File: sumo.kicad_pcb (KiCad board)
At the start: 2 copper layers, 76.2 x 94 mm, 55 parts, among them Q1 BPW40, Q2 BPW40, SW1 SW_Push, SW2 SW_DIP_x01, SW3 SW_DIP_x01, SW4 SW_DIP_x01, T1 Screw_Terminal_01x04, T2 Screw_Terminal_01x04, T3 Screw_Terminal_01x04, T4 Screw_Terminal_01x04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

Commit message: save changes
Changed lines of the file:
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@@
 			)
 		)
-		(pad "1" thru_hole rect
+		(pad "1" thru_hole circle
 			(at 0 0 270)
-			(size 1.4 1.4)
-			(drill 0.7)
+			(size 1.778 1.778)
+			(drill 0.8)
 			(layers "*.Cu" "*.Mask")
 			(remove_unused_layers no)
@@
 			)
 		)
-		(pad "1" thru_hole rect
+		(pad "1" thru_hole circle
 			(at 0 0 270)
-			(size 1.4 1.4)
-			(drill 0.7)
+			(size 1.778 1.778)
+			(drill 0.8)
 			(layers "*.Cu" "*.Mask")
 			(remove_unused_layers no)
@@
 			)
 		)
-		(pad "1" thru_hole rect
+		(pad "1" thru_hole circle
 			(at 0 0)
-			(size 1.4 1.4)
-			(drill 0.7)
+			(size 1.778 1.778)
+			(drill 0.8)
 			(layers "*.Cu" "*.Mask")
 			(remove_unused_layers no)

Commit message: finishing touches
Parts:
- moved T5 1.27 mm to (154.9, 83.8)
- moved T3 1.27 mm to (176.5, 114.3)
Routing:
- net Net-(T5-Pin_1): track 33.7 -> 32.4 mm
- net Net-(T5-Pin_4): track 21.2 -> 19.9 mm
- net Net-(T5-Pin_3): track 23.7 -> 22.4 mm
- net Net-(T5-Pin_2): track 31.9 -> 30.7 mm
- net Net-(C4-Pad1): track 48.8 -> 49.9 mm
- net Net-(U4-Pad2): track 35.7 -> 36.6 mm
- net Net-(T3-Pin_4): track 6.89 -> 6.36 mm
- net Net-(T3-Pin_3): track 7.41 -> 6.89 mm
- net Net-(T3-Pin_2): track 6.89 -> 7.41 mm
- net Net-(T3-Pin_1): track 6.36 -> 6.89 mm
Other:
- board text added: "Vacuum Cleaner Motherboard"
- board text added: "Vacuum Cleaner Sensor board"

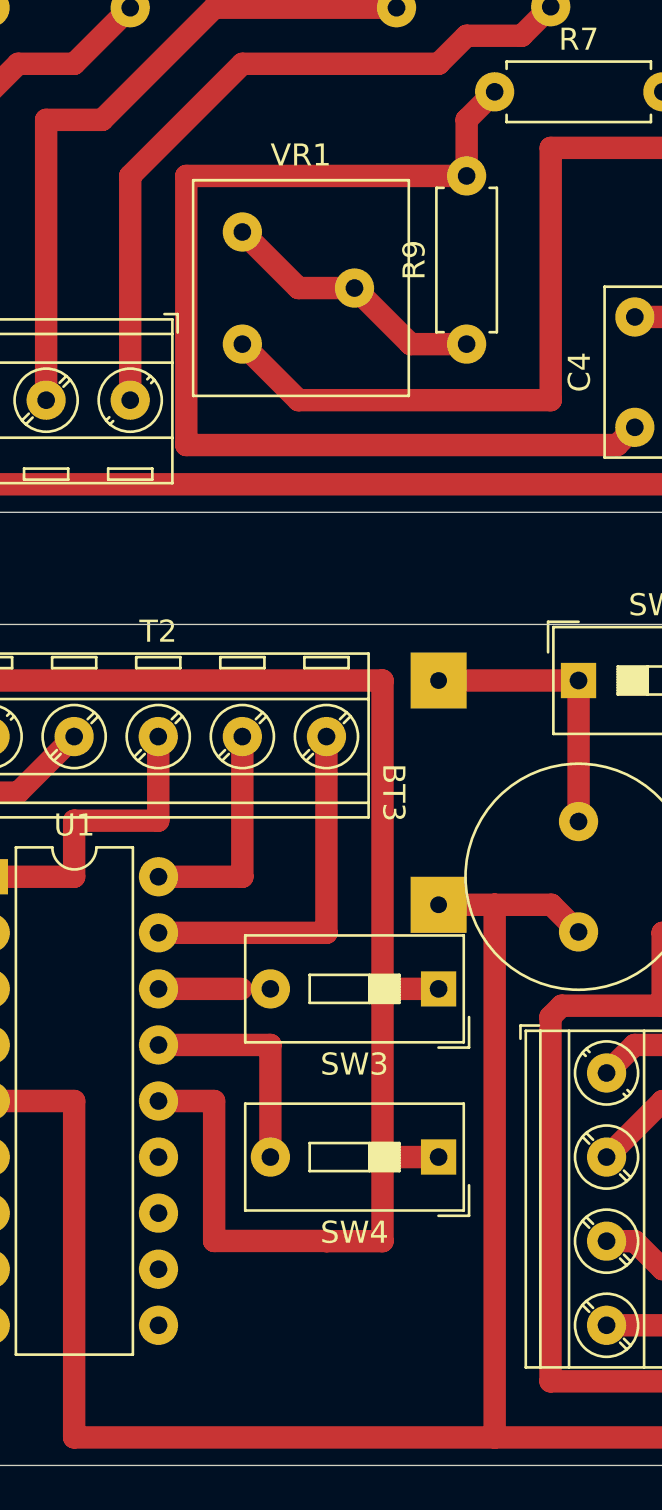
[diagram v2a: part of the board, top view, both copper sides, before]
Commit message: add pull up resistor to switch inputs
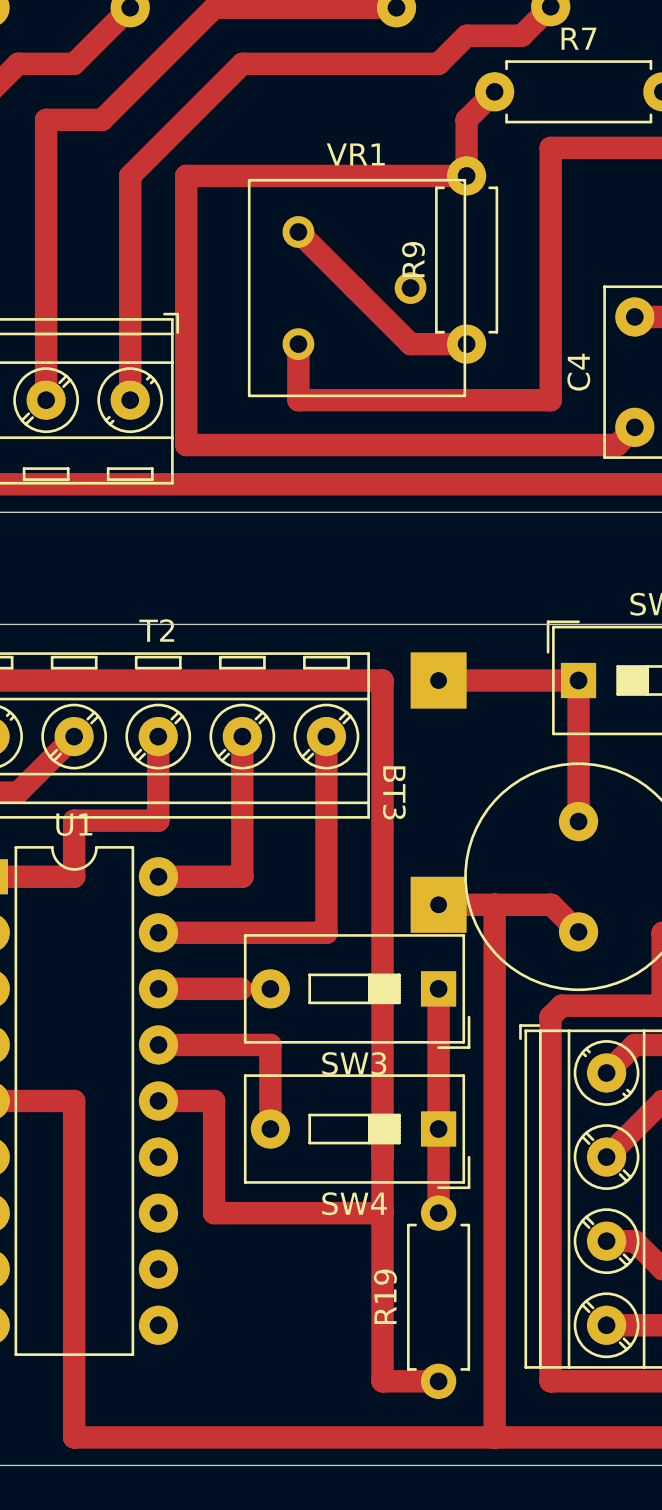
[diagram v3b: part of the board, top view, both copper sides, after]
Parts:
- added R19: 4.7k, Resistor_THT:R_Axial_DIN0207_L6.3mm_D2.5mm_P7.62mm_Horizontal, F.Cu at (168.9, 128.3)
- moved VR1 2.54 mm to (162.6, 81.3)
- moved SW4 1.27 mm to (168.9, 116.8)
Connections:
- SW3 pad 1: +5V -> Net-(R19-Pad2)
- SW4 pad 1: +5V -> Net-(R19-Pad2)
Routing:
- net Net-(R19-Pad2): track 0.00 -> 10.2 mm
- net +5V: track 91.2 -> 95.0 mm
- net Net-(R9-Pad1): track 12.3 -> 9.72 mm
- net Net-(U1-CLKOUT/OSC2/RA6): track 10.1 -> 8.88 mm
- net Net-(U4-Pad2): track 36.6 -> 35.6 mm

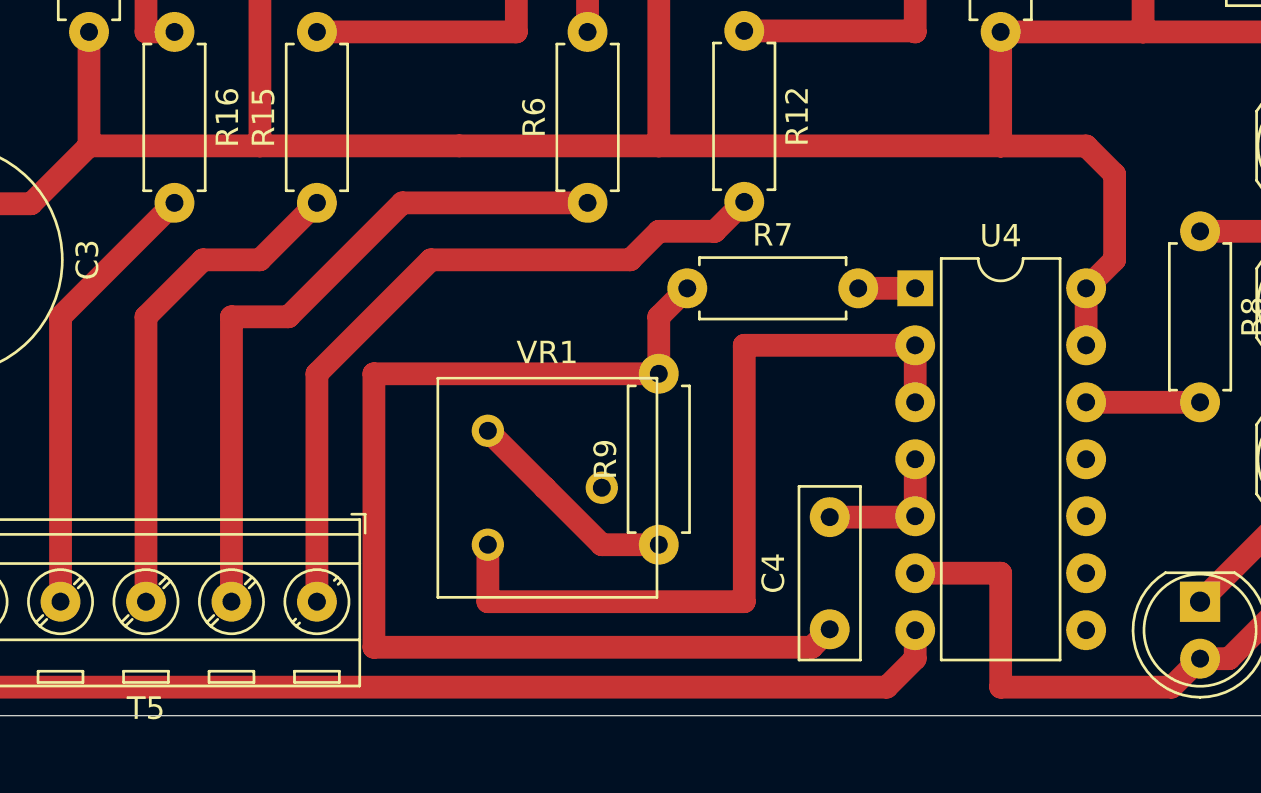
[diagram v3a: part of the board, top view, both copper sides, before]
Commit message: change potentiometer footprint
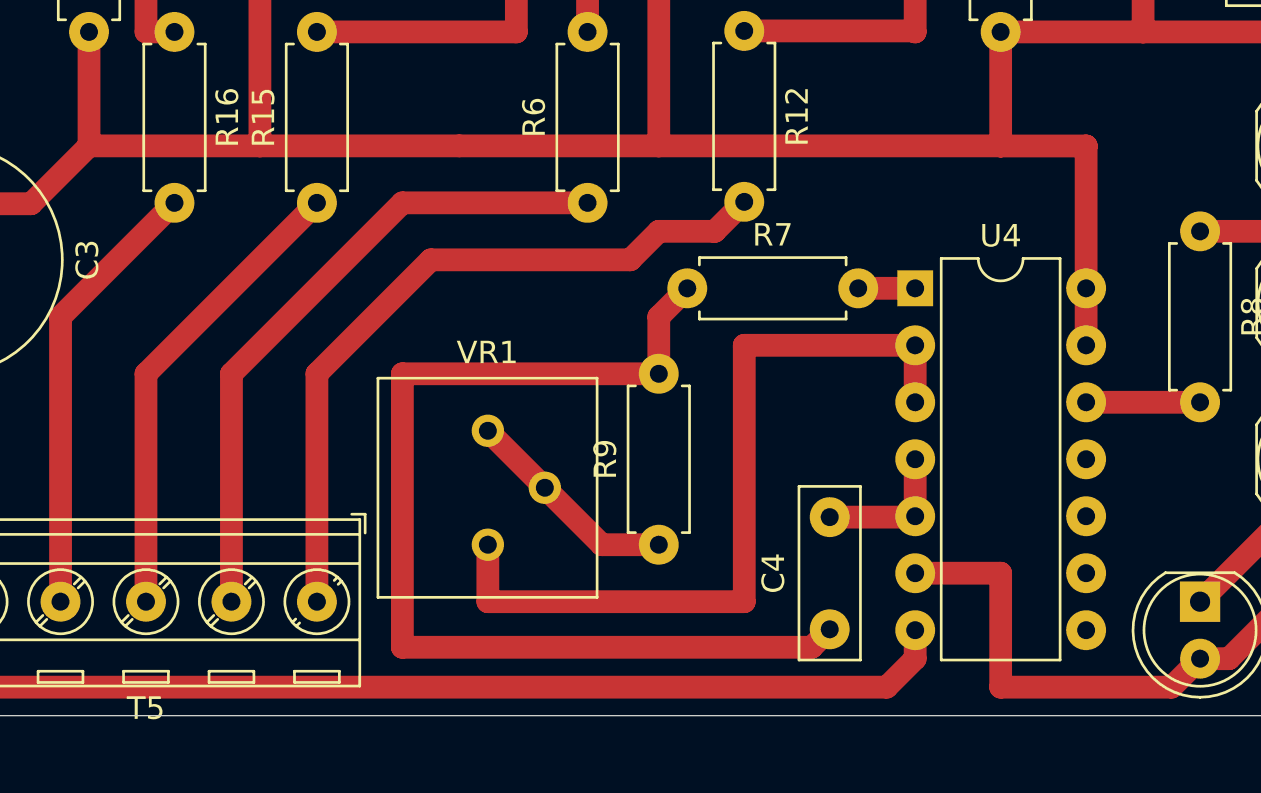
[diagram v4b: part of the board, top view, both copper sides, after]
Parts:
- R19: value 4.7k -> 1k
- VR1: footprint Potentiometer_THT:Potentiometer_Bourns_3386F_Vertical -> Potentiometer_THT:Potentiometer_Bourns_3386P_Vertical
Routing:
- net Net-(C4-Pad1): track 49.9 -> 47.3 mm
- net Net-(T5-Pin_3): track 22.4 -> 20.9 mm
- net Net-(T5-Pin_2): track 30.7 -> 29.2 mm
- net +6V: track 150.9 -> 149.9 mm

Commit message: ground plane
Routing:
- net GNDREF: track 358.0 -> 0.08 mm
- net Net-(D3-A): track 44.6 -> 47.5 mm
- net +6V: track 149.9 -> 147.2 mm
- net Net-(D3-K): track 25.7 -> 27.9 mm
- net Net-(Q2-C): track 24.4 -> 26.7 mm
- net Net-(Q1-C): track 15.3 -> 17.1 mm
- net Net-(T2-Pin_2): track 14.7 -> 16.3 mm
- net Net-(U1-CLKIN/OSC1/RA7): track 3.76 -> 5.07 mm
- net +5V: track 95.0 -> 93.8 mm
- net Net-(U3-VCC1): track 85.6 -> 86.6 mm
- net Net-(U1-~{MCLR}/Vpp/RA5): track 13.2 -> 14.0 mm
- net Net-(C4-Pad1): track 47.3 -> 48.1 mm
- added copper zone on F.Cu, net GNDREF

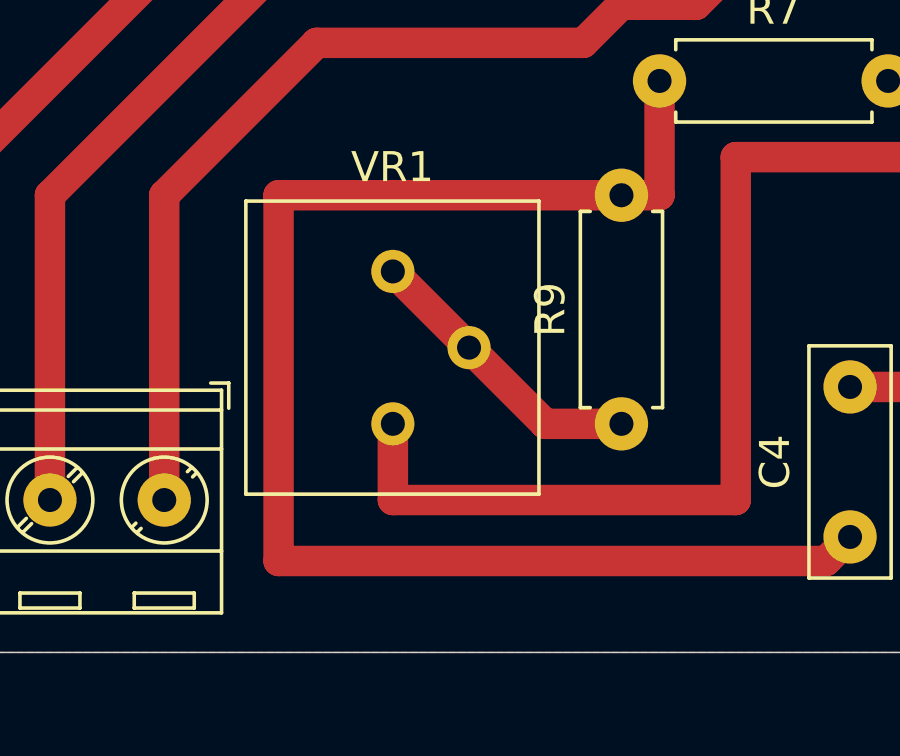
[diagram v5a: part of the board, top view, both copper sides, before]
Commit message: change potentiometer pads
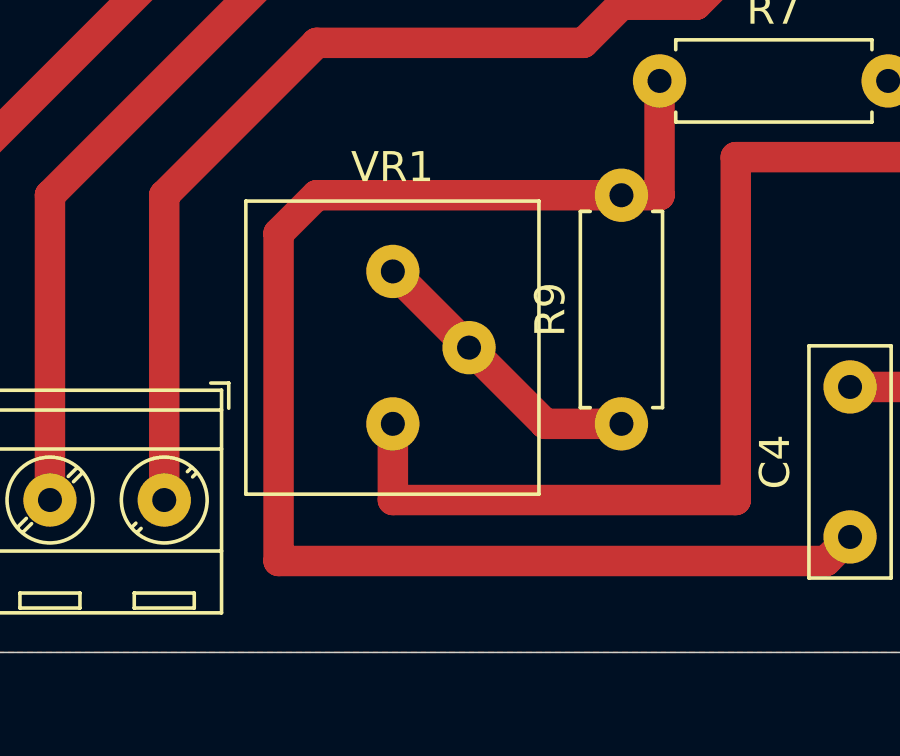
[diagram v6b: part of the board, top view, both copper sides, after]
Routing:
- net Net-(C4-Pad1): track 48.1 -> 47.3 mm
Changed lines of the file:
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@@
 		(pad "1" thru_hole circle
 			(at 0 0)
-			(size 1.44 1.44)
+			(size 1.778 1.778)
 			(drill 0.8)
 			(layers "*.Cu" "*.Mask")
@@
 		(pad "2" thru_hole circle
 			(at 2.54 -2.54)
-			(size 1.44 1.44)
+			(size 1.778 1.778)
 			(drill 0.8)
 			(layers "*.Cu" "*.Mask")
@@
 		(pad "3" thru_hole circle
 			(at 0 -5.08)
-			(size 1.44 1.44)
+			(size 1.778 1.778)
 			(drill 0.8)
 			(layers "*.Cu" "*.Mask")
@@
 	)
 	(segment
-		(start 176.998 85.852)
-		(end 177.8 85.05)
+		(start 158.75 85.852)
+		(end 176.998 85.852)
 		(width 1.016)
 		(layer "F.Cu")
@@
 	)
 	(segment
-		(start 158.75 85.852)
-		(end 176.998 85.852)
+		(start 160.02 73.66)
+		(end 158.75 74.93)
+		(width 1.016)
+		(layer "F.Cu")
+		(net 25)
+	)
+	(segment
+		(start 170.18 73.66)
+		(end 160.02 73.66)
 		(width 1.016)
 		(layer "F.Cu")
@@
 	)
 	(segment
-		(start 158.75 73.66)
-		(end 158.75 85.852)
+		(start 176.998 85.852)
+		(end 177.8 85.05)
 		(width 1.016)
 		(layer "F.Cu")
@@
 	)
 	(segment
-		(start 170.18 73.66)
-		(end 158.75 73.66)
+		(start 158.75 74.93)
+		(end 158.75 85.852)
 		(width 1.016)
 		(layer "F.Cu")

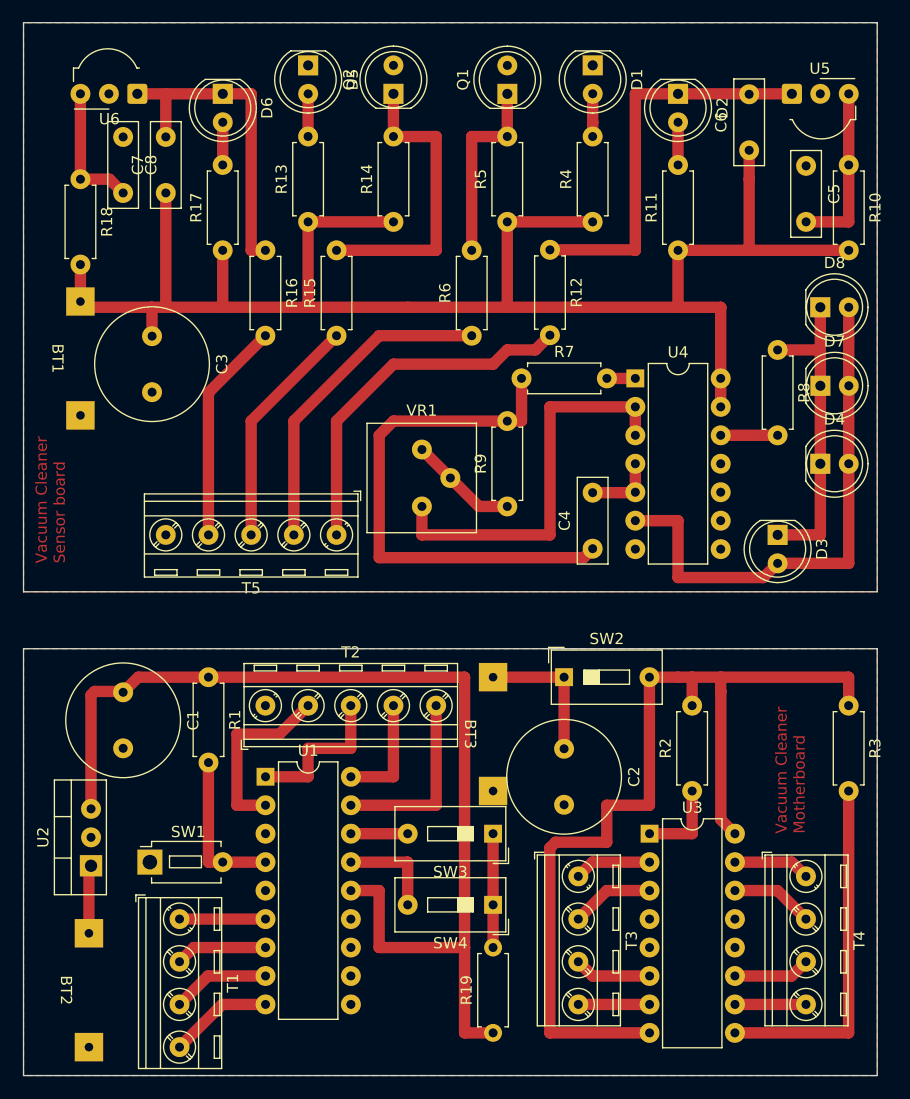
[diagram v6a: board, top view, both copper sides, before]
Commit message: remove ground plane
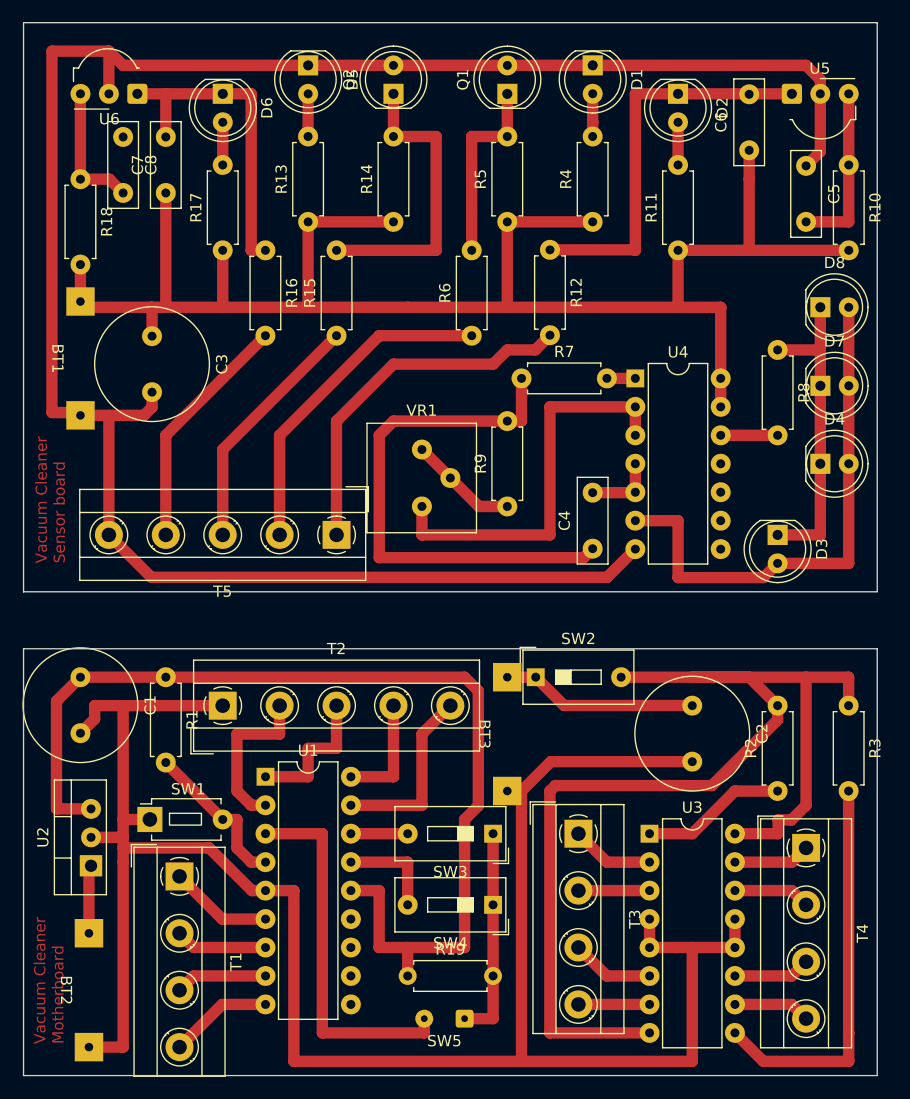
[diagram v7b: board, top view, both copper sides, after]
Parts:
- added SW5: SW_DIP_x01, Connector_Wire:SolderWire-0.1sqmm_1x02_P3.6mm_D0.4mm_OD1mm, F.Cu at (166.4, 127.0)
- T1, T3, T4: footprint TerminalBlock_MetzConnect:TerminalBlock_MetzConnect_Type086_RT03404HBLC_1x04_P3.81mm_Horizontal -> TerminalBlock_MetzConnect:TerminalBlock_MetzConnect_Type101_RT01604HBWC_1x04_P5.08mm_Horizontal
- T2, T5: value Screw_Terminal_01x04 -> Screw_Terminal_01x05; footprint TerminalBlock_MetzConnect:TerminalBlock_MetzConnect_Type086_RT03405HBLC_1x05_P3.81mm_Horizontal -> TerminalBlock_MetzConnect:TerminalBlock_MetzConnect_Type101_RT01605HBWC_1x05_P5.08mm_Horizontal
- moved C2 12.1 mm to (186.7, 99.1)
- moved R19 9.16 mm to (161.3, 123.2), turned to 0 degrees
- moved R2 7.63 mm to (194.3, 106.7)
- moved C1 4.04 mm to (132.1, 96.5)
- moved T3 3.81 mm to (176.5, 110.5)
- moved R1 3.81 mm to (139.7, 96.5)
- moved SW1 3.81 mm to (138.3, 109.2)
- moved T1 3.81 mm to (140.9, 114.3)
- moved T2 3.81 mm to (144.8, 99.1)
- moved T4 2.54 mm to (196.8, 111.8)
- moved SW2 2.53 mm to (172.7, 96.5)
- moved BT3 1.27 mm to (167.6, 101.6)
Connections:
- U1 pad 3: unconnected-(U1-TOCKI/CMP2/RA4-Pad3) -> Net-(U1-TOCKI/CMP2/RA4)
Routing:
- net GNDREF: track 0.08 -> 370.3 mm
- net Net-(U1-TOCKI/CMP2/RA4): track 0.00 -> 33.2 mm
- net Net-(U3-VCC1): track 86.6 -> 105.8 mm
- net Net-(R19-Pad2): track 10.2 -> 19.0 mm
- net Net-(U3-EN1,2): track 7.61 -> 13.0 mm
- net Net-(BT3-+): track 12.7 -> 17.6 mm
- net Net-(U3-EN3,4): track 31.7 -> 35.3 mm
- net Net-(T2-Pin_2): track 16.3 -> 14.5 mm
- net Net-(T5-Pin_4): track 19.9 -> 21.5 mm
- net Net-(T1-Pin_1): track 7.67 -> 9.25 mm
- net Net-(T2-Pin_3): track 14.0 -> 12.7 mm
- net Net-(T3-Pin_2): track 7.41 -> 6.35 mm
- net Net-(T5-Pin_3): track 20.9 -> 22.0 mm
- net +5V: track 93.8 -> 92.9 mm
- net Net-(T4-Pin_4): track 6.34 -> 6.88 mm
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- removed copper zone on F.Cu, net GNDREF
